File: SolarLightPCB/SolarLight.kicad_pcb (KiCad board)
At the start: 2 copper layers, 100 x 45 mm, 19 parts, among them J1 I2C, J2 SPI, SW1 RotaryEncoder_Switch, U1 TP4056, U2 WeMos_D1_mini, U3 MCP1700-3302E

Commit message: Add GND Jumper
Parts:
- added JP6: Jumper_2_Bridged, Resistor_THT:R_Axial_DIN0204_L3.6mm_D1.6mm_P5.08mm_Horizontal, F.Cu at (127.6, 96.7)
- moved G*** 37.9 mm to (105.0, 75.0)
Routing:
- net GND: track 0.00 -> 3.03 mm
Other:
- board text added: "v0.4 - 03.11.2022"
- board text removed: "v0.3 - 24.10.2022"
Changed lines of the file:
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@@
   (net 19 "Net-(SC1-Pad1)")
   (net 20 "A0")
-  (net 21 "Net-(U2-Pad13)")
+  (net 21 "Net-(JP3-Pad2)")
   (net 22 "ROTARY_A")
-  (net 23 "Net-(U2-Pad14)")
+  (net 23 "Net-(JP4-Pad2)")
   (net 24 "ROTARY_B")
   (net 25 "ROTARY_SWITCH")
@@
       (net 4 "GND") (pinfunction "Pin_4") (pintype "passive"))
     (model "${KICAD6_3DMODEL_DIR}/Connector_PinHeader_2.54mm.3dshapes/PinHeader_1x04_P2.54mm_Vertical.wrl"
+      (offset (xyz 0 0 0))
+      (scale (xyz 1 1 1))
+      (rotate (xyz 0 0 0))
+    )
+  )
+  (footprint "Resistor_THT:R_Axial_DIN0204_L3.6mm_D1.6mm_P5.08mm_Horizontal" (layer "F.Cu")
+    (at 127.635 96.7232)
+    (descr "Resistor, Axial_DIN0204 series, Axial, Horizontal, pin pitch=5.08mm, 0.167W, length*diameter=3.6*1.6mm^2, http://cdn-reichelt.de/documents/datenblatt/B400/1_4W%23YAG.pdf")
+    (tags "Resistor Axial_DIN0204 series Axial Horizontal pin pitch 5.08mm 0.167W length 3.6mm diameter 1.6mm")
+    (property "Sheetfile" "SolarLight.kicad_sch")
+    (property "Sheetname" "")
+    (attr through_hole)
+    (fp_text reference "JP6" (at 2.54 -1.92) (layer "F.SilkS")
+      (effects (font (size 1 1) (thickness 0.15)))
+    )
+    (fp_text value "Jumper_2_Bridged" (at 2.54 1.92) (layer "F.Fab")
+      (effects (font (size 1 1) (thickness 0.15)))
+    )
+    (fp_text user "${REFERENCE}" (at 2.54 0) (layer "F.Fab")
+      (effects (font (size 0.72 0.72) (thickness 0.108)))
+    )
+    (fp_line (start 0.62 -0.92) (end 4.46 -0.92) (layer "F.SilkS") (width 0.12))
+    (fp_line (start 0.62 0.92) (end 4.46 0.92) (layer "F.SilkS") (width 0.12))
+    (fp_line (start 6.03 1.05) (end 6.03 -1.05) (layer "F.CrtYd") (width 0.05))
+    (fp_line (start -0.95 1.05) (end 6.03 1.05) (layer "F.CrtYd") (width 0.05))
+    (fp_line (start -0.95 -1.05) (end -0.95 1.05) (layer "F.CrtYd") (width 0.05))
+    (fp_line (start 6.03 -1.05) (end -0.95 -1.05) (layer "F.CrtYd") (width 0.05))
+    (fp_line (start 0.74 -0.8) (end 0.74 0.8) (layer "F.Fab") (width 0.1))
+    (fp_line (start 5.08 0) (end 4.34 0) (layer "F.Fab") (width 0.1))
+    (fp_line (start 4.34 0.8) (end 4.34 -0.8) (layer "F.Fab") (width 0.1))
+    (fp_line (start 0.74 0.8) (end 4.34 0.8) (layer "F.Fab") (width 0.1))
+    (fp_line (start 0 0) (end 0.74 0) (layer "F.Fab") (width 0.1))
+    (fp_line (start 4.34 -0.8) (end 0.74 -0.8) (layer "F.Fab") (width 0.1))
+    (pad "1" thru_hole circle (at 0 0) (size 1.4 1.4) (drill 0.7) (layers *.Cu *.Mask)
+      (net 4 "GND") (pinfunction "A") (pintype "passive"))
+    (pad "2" thru_hole oval (at 5.08 0) (size 1.4 1.4) (drill 0.7) (layers *.Cu *.Mask)
+      (net 4 "GND") (pinfunction "B") (pintype "passive"))
+    (model "${KICAD6_3DMODEL_DIR}/Resistor_THT.3dshapes/R_Axial_DIN0204_L3.6mm_D1.6mm_P5.08mm_Horizontal.wrl"
       (offset (xyz 0 0 0))
       (scale (xyz 1 1 1))
@@
       (net 25 "ROTARY_SWITCH") (pinfunction "D3") (pintype "bidirectional"))
     (pad "13" thru_hole oval (at 22.86 7.62 270) (size 3 1.6) (drill 1) (layers *.Cu *.Mask)
-      (net 21 "Net-(U2-Pad13)") (pinfunction "SDA/D2") (pintype "bidirectional"))
+      (net 21 "Net-(JP3-Pad2)") (pinfunction "SDA/D2") (pintype "bidirectional"))
     (pad "14" thru_hole oval (at 22.86 5.08 270) (size 3 1.6) (drill 1) (layers *.Cu *.Mask)
-      (net 23 "Net-(U2-Pad14)") (pinfunction "SCL/D1") (pintype "bidirectional"))
+      (net 23 "Net-(JP4-Pad2)") (pinfunction "SCL/D1") (pintype "bidirectional"))
     (pad "15" thru_hole oval (at 22.86 2.54 270) (size 3 1.6) (drill 1) (layers *.Cu *.Mask)
       (net 16 "unconnected-(U2-Pad15)") (pinfunction "RX") (pintype "input+no_connect"))
@@
   )
   (footprint "LOGO" (layer "F.Cu")
-    (at 132.857542 49.236993)
+    (at 105 75)
     (attr board_only exclude_from_pos_files exclude_from_bom)
     (fp_text reference "G***" (at 0 0) (layer "F.SilkS") hide
@@
       (net 15 "SCL") (pinfunction "A") (pintype "passive"))
     (pad "2" smd rect (at 0 0 90) (size 1 1.5) (layers "B.Cu" "B.Mask")
-      (net 23 "Net-(U2-Pad14)") (pinfunction "C") (pintype "passive"))
+      (net 23 "Net-(JP4-Pad2)") (pinfunction "C") (pintype "passive"))
     (pad "3" smd rect (at 1.3 0 90) (size 1 1.5) (layers "B.Cu" "B.Mask")
       (net 22 "ROTARY_A") (pinfunction "B") (pintype "passive"))
@@
       (net 14 "SDA") (pinfunction "A") (pintype "passive"))
     (pad "2" smd rect (at 0 0 270) (size 1 1.5) (layers "B.Cu" "B.Mask")
-      (net 21 "Net-(U2-Pad13)") (pinfunction "C") (pintype "passive"))
+      (net 21 "Net-(JP3-Pad2)") (pinfunction "C") (pintype "passive"))
     (pad "3" smd rect (at 1.3 0 270) (size 1 1.5) (layers "B.Cu" "B.Mask")
       (net 24 "ROTARY_B") (pinfunction "B") (pintype "passive"))
@@
       (net 7 "RST") (pinfunction "B") (pintype "passive"))
   )
+  (gr_rect (start 170 74) (end 85 82) (layer "B.SilkS") (width 0.1) (fill none))
   (gr_circle (center 175 59) (end 176.5 59) (layer "Edge.Cuts") (width 0.1) (fill none))
   (gr_circle (center 84 96) (end 85.5 96) (layer "Edge.Cuts") (width 0.1) (fill none))
@@
   (gr_circle (center 175 96) (end 176.5 96) (layer "Edge.Cuts") (width 0.1) (fill none))
   (gr_rect (start 80 100) (end 180 55) (layer "Edge.Cuts") (width 0.1) (fill none))
-  (gr_rect (start 170 74) (end 85 82) (layer "F.Fab") (width 0.1) (fill none))
-  (gr_text "v0.3 - 24.10.2022" (at 157 98) (layer "F.SilkS")
+  (gr_text "v0.4 - 03.11.2022" (at 157 98) (layer "F.SilkS")
     (effects (font (size 1.5 1.5) (thickness 0.3)))
   )
@@
   (segment (start 153.9452 68) (end 139.0396 82.9056) (width 0.8) (layer "B.Cu") (net 3))
   (segment (start 123.404 90.508) (end 123.404 89.408) (width 0.8) (layer "B.Cu") (net 3))
+  (segment (start 128.026 93.853) (end 128.026 96.3322) (width 0.8) (layer "B.Cu") (net 4))
+  (segment (start 128.026 96.3322) (end 127.635 96.7232) (width 0.8) (layer "B.Cu") (net 4))
   (segment (start 93.3704 81.9404) (end 93.3704 88.9278) (width 0.8) (layer "B.Cu") (net 5))
   (segment (start 89.43 78) (end 93.3704 81.9404) (width 0.8) (layer "B.Cu") (net 5))
@@
   (segment (start 118.859 85) (end 120.7408 83.1182) (width 0.8) (layer "B.Cu") (net 25))
   (segment (start 99.1382 85) (end 118.859 85) (width 0.8) (layer "B.Cu") (net 25))
-  (segment (start 143.2575 61.6712) (end 144.8308 61.6712) (width 0.8) (layer "B.Cu") (net 26))
-  (segment (start 141.9606 61.595) (end 143.1813 61.595) (width 0.8) (layer "B.Cu") (net 26))
-  (segment (start 143.1813 61.595) (end 143.2575 61.6712) (width 0.8) (layer "B.Cu") (net 26))
-  (segment (start 138.2268 65.3288) (end 141.9606 61.595) (width 0.8) (layer "B.Cu") (net 26))
+  (segment (start 141.8844 61.6712) (end 144.8308 61.6712) (width 0.8) (layer "B.Cu") (net 26))
+  (segment (start 138.2268 65.3288) (end 141.8844 61.6712) (width 0.8) (layer "B.Cu") (net 26))
   (segment (start 127.2964 65.3288) (end 138.2268 65.3288) (width 0.8) (layer "B.Cu") (net 26))
   (segment (start 164 61) (end 165.599 61) (width 0.8) (layer "B.Cu") (net 27))

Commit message: Make a “simplified” version
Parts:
- removed JP1: Deep Sleep, Jumper:SolderJumper-2_P1.3mm_Bridged_Pad1.0x1.5mm
- removed JP2, JP6: Jumper_2_Bridged, Resistor_THT:R_Axial_DIN0204_L3.6mm_D1.6mm_P5.08mm_Horizontal
- removed JP3, JP4: SolderJumper_3_Bridged12, Jumper:SolderJumper-3_P1.3mm_Bridged12_Pad1.0x1.5mm
- removed JP5: POWER ON, Connector_PinHeader_2.54mm:PinHeader_1x02_P2.54mm_Vertical
- BT1, SC1: footprint Connector_PinHeader_2.54mm:PinHeader_1x02_P2.54mm_Vertical -> TerminalBlock_Phoenix:TerminalBlock_Phoenix_PT-1,5-2-3.5-H_1x02_P3.50mm_Horizontal
- J2: value SPI -> Conn_01x06_Male
- SW1: value RotaryEncoder_Switch -> SW_Push; footprint Rotary_Encoder:RotaryEncoder_Alps_EC12E-Switch_Vertical_H20mm -> Button_Switch_THT:SW_PUSH_6mm_H4.3mm
- moved U1 34.8 mm to (164.6, 58.4), turned to -90 degrees
- moved SW1 33.0 mm to (142.6, 64.5), turned to 180 degrees
- moved U2 27.3 mm to (123.5, 87.1), turned to 180 degrees
- moved J1 27.3 mm to (94.0, 87.0), turned to 180 degrees
- moved C1 27.0 mm to (161.4, 95.0), turned to 180 degrees
- moved U3 23.3 mm to (157.9, 90.5), turned to 0 degrees
- moved J2 14.4 mm to (130.8, 68.5), turned to 0 degrees
- moved R3 5.70 mm to (128.8, 87.6)
- moved R2 5.13 mm to (132.4, 95.2)
- moved BT1 3.49 mm to (139.8, 94.4), turned to 0 degrees
- moved SC1 3.10 mm to (148.7, 94.4), turned to 0 degrees
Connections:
- J1 pad 1: +3V3 -> SCL
- J1 pad 2: SCL -> SDA
- J1 pad 3: SDA -> +3V3
- J2 pad 3: MISO -> MOSI
- J2 pad 4: MOSI -> MISO
- J2 pad 5: Net-(J2-Pad5) -> SCK
- U2 pad 13: Net-(JP3-Pad2) -> SDA
- U2 pad 14: Net-(JP4-Pad2) -> SCL
- U2 pad 3: Net-(JP1-Pad1) -> RST
- U3 pad 3: Net-(JP5-Pad1) -> +3V3
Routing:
- net MOSI: track 62.4 -> 7.71 mm
- net MISO: track 59.4 -> 7.71 mm
- net +3V3: track 203.1 -> 158.3 mm
- net Net-(SC1-Pad1): track 30.7 -> 70.5 mm
- net A0: track 50.5 -> 13.0 mm
- net Net-(BT1-Pad2): track 19.7 -> 54.5 mm
- net ROTARY_B: track 27.1 -> 0.00 mm
- net Net-(U1-Pad3): track 27.9 -> 6.04 mm
- net Net-(JP3-Pad2): track 20.9 -> 0.00 mm
- net SCK: track 27.5 -> 7.71 mm
- net CS: track 59.7 -> 40.4 mm
- net Net-(J2-Pad5): track 19.0 -> 0.00 mm
- net Net-(JP4-Pad2): track 17.1 -> 0.00 mm
- net ROTARY_SWITCH: track 35.9 -> 49.9 mm
- net Neopixel: track 16.5 -> 29.9 mm
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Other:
- board size 100 x 45 mm -> 95 x 45 mm
- board text added: "- rotate the ESP and place it centered - then stuff stuff on either side - add a switch to change some modes - change the width to fit the neopixel - changed hole size to be 1mm except a small one from the transistor - only create the hole-map and delete the small file. - add the spi again - removed rotary encoder"
- board text added: "FablabZurich"

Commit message: Updated the simple pcb
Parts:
- added SW2: ON_OFF, Connector_PinHeader_2.54mm:PinHeader_1x03_P2.54mm_Vertical, F.Cu at (168.7, 89.9)
- C1: footprint Capacitor_THT:CP_Radial_D5.0mm_P2.00mm -> Capacitor_THT:CP_Radial_D5.0mm_P2.50mm
- moved SW1 54.8 mm to (87.9, 62.0), turned to 0 degrees
- moved SC1 38.9 mm to (171.7, 63.0), turned to -90 degrees
- moved C1 19.7 mm to (141.7, 94.0), turned to 0 degrees
- moved G*** 17.1 mm to (91.2, 85.1), turned to -90 degrees
- moved BT1 12.1 mm to (151.9, 95.0), turned to 180 degrees
- moved J1 11.8 mm to (104.1, 93.0), turned to -90 degrees
- moved U2 4.95 mm to (122.4, 82.3)
- moved J2 4.32 mm to (129.0, 64.5)
- moved U1 4.10 mm to (161.7, 61.3)
- moved U3 3.82 mm to (158.4, 94.3)
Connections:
- J1 pad 1: SCL -> SDA
- J1 pad 2: SDA -> SCL
- LIN1 pad 1: +3V3 -> /VOUT
- LOUT1 pad 1: +3V3 -> unconnected-(LOUT1-Pad1)
- U1 pad 3: Net-(U1-Pad3) -> /VOUT
- U3 pad 2: Net-(U1-Pad3) -> /VOUT
- U3 pad 3: +3V3 -> Net-(U3-Pad3)
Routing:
- net Net-(SC1-Pad1): track 70.5 -> 11.7 mm
- net Net-(BT1-Pad2): track 54.5 -> 9.31 mm
- net /VOUT: track 0.00 -> 28.8 mm
- net ROTARY_SWITCH: track 49.9 -> 28.6 mm
- net CS: track 40.4 -> 57.3 mm
- net +3V3: track 158.3 -> 145.6 mm
- net Neopixel: track 29.9 -> 17.5 mm
- net SCL: track 8.65 -> 20.8 mm
- net SDA: track 8.65 -> 20.7 mm
- net Net-(U3-Pad3): track 0.00 -> 7.02 mm
- net A0: track 13.0 -> 19.1 mm
- net Net-(U1-Pad3): track 6.04 -> 0.00 mm
- net RST: track 7.76 -> 9.99 mm
- net BATTERY: track 32.1 -> 33.8 mm
- net MISO: track 7.71 -> 6.60 mm
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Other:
- board text added: "v0.5 - 16.11.2022"
- board text removed: "- rotate the ESP and place it centered - then stuff stuff on either side - add a switch to change some modes - change the width to fit the neopixel - changed hole size to be 1mm except a small one from the transistor - only create the hole-map and delete the small file. - add the spi again - removed rotary encoder"
- board text removed: "FablabZurich"
- board text removed: "v0.4 - 03.11.2022"

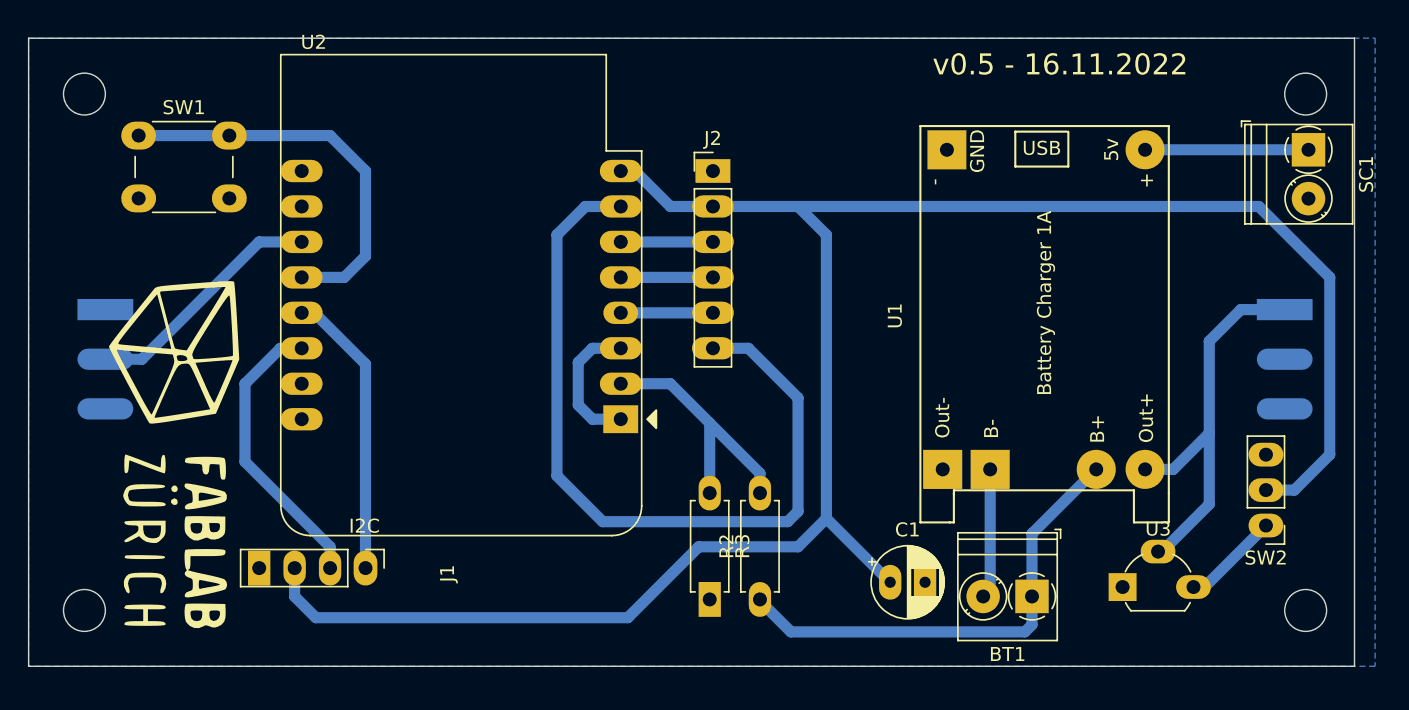
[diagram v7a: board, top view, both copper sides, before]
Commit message: Remove the voltage regulator
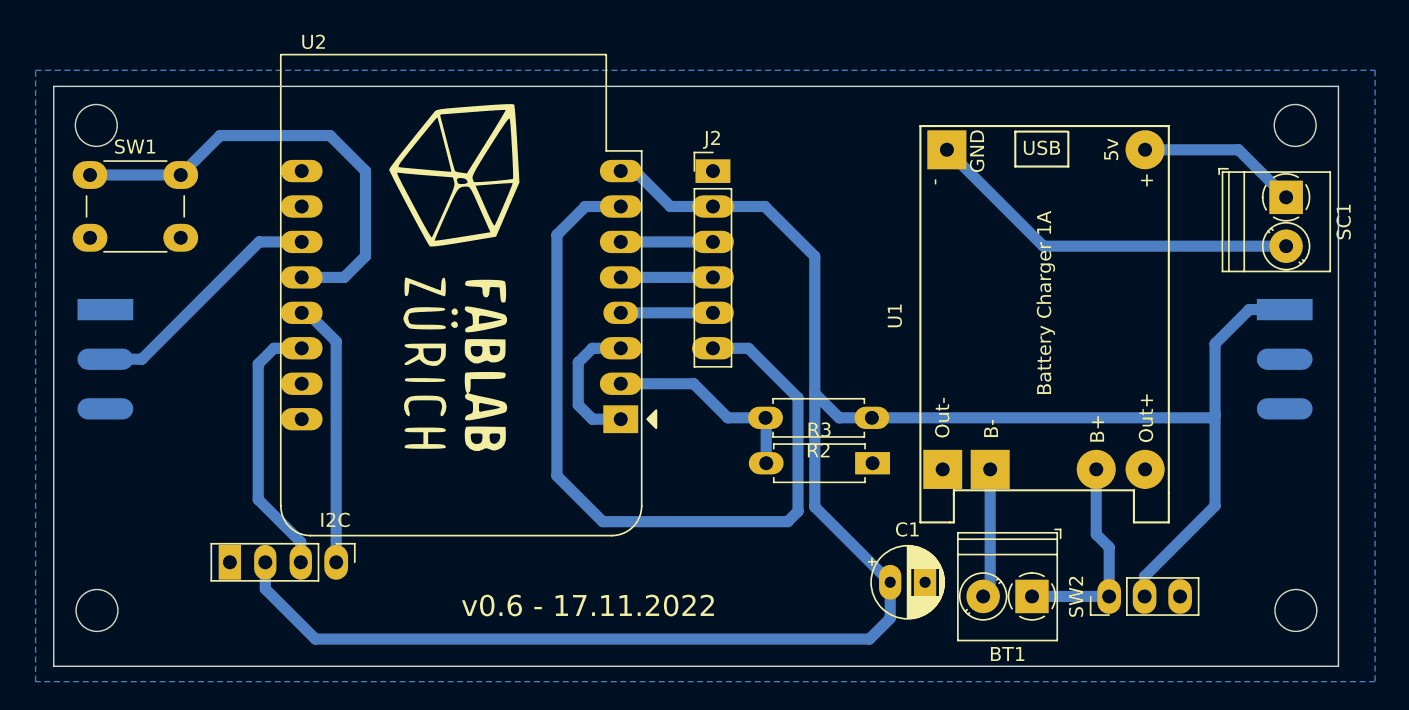
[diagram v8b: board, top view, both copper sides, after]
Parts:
- removed U3: MCP1700-3302E, Package_TO_SOT_THT:TO-92L_Wide
- moved G*** 23.7 mm to (111.3, 72.4)
- moved R2 15.3 mm to (140.4, 82.2), turned to 180 degrees
- moved SW2 12.3 mm to (157.4, 95.0), turned to 90 degrees
- moved R3 4.58 mm to (132.8, 85.5), turned to 0 degrees
- moved SW1 4.48 mm to (84.4, 64.8)
- moved SC1 3.77 mm to (170.1, 66.4)
- moved J1 2.14 mm to (102.0, 92.5)
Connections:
- net ROTARY_SWITCH renamed SWITCH
- BT1 pad 1: BATTERY -> Net-(BT1-Pad1)
- BT1 pad 2: Net-(BT1-Pad2) -> GND
- C1 pad 1: +3V3 -> BATTERY
- J1 pad 3: +3V3 -> BATTERY
- J2 pad 2: +3V3 -> BATTERY
- LIN1 pad 1: /VOUT -> BATTERY
- SC1 pad 2: GND -> Net-(SC1-Pad2)
- SW2 pad 1: Net-(U3-Pad3) -> Net-(BT1-Pad1)
- SW2 pad 2: +3V3 -> BATTERY
- U1 pad 2: GND -> Net-(SC1-Pad2)
- U1 pad 3: /VOUT -> unconnected-(U1-Pad3)
- U1 pad 4: GND -> unconnected-(U1-Pad4)
- U1 pad 5: BATTERY -> Net-(BT1-Pad1)
- U1 pad 6: Net-(BT1-Pad2) -> GND
- U2 pad 8: +3V3 -> BATTERY
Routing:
- net +3V3: track 145.6 -> 0.00 mm
- net BATTERY: track 33.8 -> 149.1 mm
- net /VOUT: track 28.8 -> 0.00 mm
- net Net-(SC1-Pad2): track 0.00 -> 27.2 mm
- net Net-(BT1-Pad1): track 0.00 -> 15.0 mm
- net Net-(BT1-Pad2): track 9.31 -> 0.00 mm
- net GND: track 0.00 -> 9.31 mm
- net Net-(U3-Pad3): track 7.02 -> 0.00 mm
- net SWITCH: track 28.6 -> 33.3 mm
- net A0: track 19.1 -> 14.7 mm
- net SCL: track 20.8 -> 19.1 mm
- net SDA: track 20.7 -> 19.1 mm
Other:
- board size 95 x 45 mm -> 92 x 41.5 mm
- board text added: "v0.6 - 17.11.2022"
- board text removed: "v0.5 - 16.11.2022"
